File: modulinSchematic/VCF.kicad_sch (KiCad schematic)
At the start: 0 parts

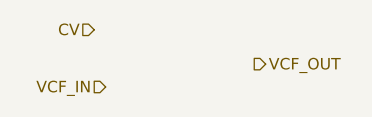
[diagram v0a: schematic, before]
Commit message: Add power schematic
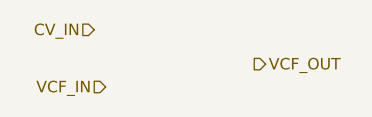
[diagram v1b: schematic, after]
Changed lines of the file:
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@@
 	(generator_version "9.0")
 	(paper "A4")
-	(hierarchical_label "CV"
+	(hierarchical_label "CV_IN"
 		(shape input)
 		(at 64.77 38.1 180)
